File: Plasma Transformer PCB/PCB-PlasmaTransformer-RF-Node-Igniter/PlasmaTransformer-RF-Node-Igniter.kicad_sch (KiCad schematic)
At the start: 66 parts, among them J1 Barrel_Jack_MountingPin, J11 Screw_Terminal_01x01, J12 Screw_Terminal_01x01, J2 Conn_01x02_Pin, J3 Conn_Coaxial, J4 Conn_02x04_Odd_Even, J5 Conn_Coaxial, J8 AudioJack3, M1 Fan, Q1 Q_NMOS_Depletion_GDS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

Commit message: adding PDF schematic
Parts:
- D5, D6, D7, D8: value D_Schottky -> D; symbol Device:D_Schottky -> Device:D; MPN ADS12B3-ASARH -> VS-E7FX0112-M3/I; Manufacturer Luminus Devices -> Vishay
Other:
- note added: "Recommended Resonant Cap: 20cm Globe: 3x 24pF 564RC0GAJ602EJ240J 13cm Globe: 5x 12pF CGP1C120KNSDAAWL25"
- note removed: "Recommended Resonant Cap: 20cm Globe: 2x 24pF 564RC0GAJ602EJ240J 13cm Globe: 5x 12pF CGP1C120KNSDAAWL25"
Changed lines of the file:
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@@
 		)
 	)
-	(text "Recommended Resonant Cap:\n20cm Globe: 2x 24pF 564RC0GAJ602EJ240J\n13cm Globe: 5x 12pF CGP1C120KNSDAAWL25"
+	(text "Recommended Resonant Cap:\n20cm Globe: 3x 24pF 564RC0GAJ602EJ240J\n13cm Globe: 5x 12pF CGP1C120KNSDAAWL25"
 		(exclude_from_sim no)
 		(at 225.806 95.25 0)
@@
 	)
 	(symbol
-		(lib_id "Device:D_Schottky")
+		(lib_id "Device:D")
 		(at 238.76 52.07 0)
 		(unit 1)
@@
 			)
 		)
-		(property "Value" "D_Schottky"
+		(property "Value" "D"
 			(at 238.4425 48.26 0)
 			(effects
@@
 			)
 		)
-		(property "Description" "Schottky diode"
+		(property "Description" "Diode"
+			(at 238.76 52.07 0)
+			(effects
+				(font
+					(size 1.27 1.27)
+				)
+				(hide yes)
+			)
+		)
+		(property "MPN" "VS-E7FX0112-M3/I"
+			(at 239.522 54.61 0)
+			(effects
+				(font
+					(size 1.27 1.27)
+				)
+			)
+		)
+		(property "Manufacturer" "Vishay"
 			(at 238.76 52.07 0)
 			(effects
@@
 			)
 		)
-		(property "MPN" "ADS12B3-ASARH"
+		(property "Sim.Device" "D"
 			(at 238.76 52.07 0)
 			(effects
@@
 			)
 		)
-		(property "Manufacturer" "Luminus Devices"
+		(property "Sim.Pins" "1=K 2=A"
 			(at 238.76 52.07 0)
 			(effects
@@
 	)
 	(symbol
-		(lib_id "Device:D_Schottky")
+		(lib_id "Device:D")
 		(at 238.76 48.26 180)
 		(unit 1)
@@
 			)
 		)
-		(property "Value" "D_Schottky"
+		(property "Value" "D"
 			(at 239.0775 52.07 0)
 			(effects
@@
 			)
 		)
-		(property "Description" "Schottky diode"
+		(property "Description" "Diode"
 			(at 238.76 48.26 0)
 			(effects
@@
 			)
 		)
-		(property "MPN" "ADS12B3-ASARH"
+		(property "MPN" "VS-E7FX0112-M3/I"
 			(at 238.76 48.26 0)
 			(effects
@@
 			)
 		)
-		(property "Manufacturer" "Luminus Devices"
+		(property "Manufacturer" "Vishay"
+			(at 238.76 48.26 0)
+			(effects
+				(font
+					(size 1.27 1.27)
+				)
+				(hide yes)
+			)
+		)
+		(property "Sim.Device" "D"
+			(at 238.76 48.26 0)
+			(effects
+				(font
+					(size 1.27 1.27)
+				)
+				(hide yes)
+			)
+		)
+		(property "Sim.Pins" "1=K 2=A"
 			(at 238.76 48.26 0)
 			(effects
@@
 	)
 	(symbol
-		(lib_id "Device:D_Schottky")
+		(lib_id "Device:D")
 		(at 238.76 44.45 180)
 		(unit 1)
@@
 			)
 		)
-		(property "Value" "D_Schottky"
+		(property "Value" "D"
 			(at 239.0775 48.26 0)
 			(effects
@@
 			)
 		)
-		(property "Description" "Schottky diode"
+		(property "Description" "Diode"
+			(at 238.76 44.45 0)
+			(effects
+				(font
+					(size 1.27 1.27)
+				)
+				(hide yes)
+			)
+		)
+		(property "MPN" "VS-E7FX0112-M3/I"
+			(at 238.76 44.45 0)
+			(effects
+				(font
+					(size 1.27 1.27)
+				)
+				(hide yes)
+			)
+		)
+		(property "Manufacturer" "Vishay"
 			(at 238.76 44.45 0)
 			(effects
@@
 			)
 		)
-		(property "MPN" "ADS12B3-ASARH"
+		(property "Sim.Device" "D"
 			(at 238.76 44.45 0)
 			(effects
@@
 			)
 		)
-		(property "Manufacturer" "Luminus Devices"
+		(property "Sim.Pins" "1=K 2=A"
 			(at 238.76 44.45 0)
 			(effects
@@
 	)
 	(symbol
-		(lib_id "Device:D_Schottky")
+		(lib_id "Device:D")
 		(at 238.76 40.64 0)
 		(unit 1)
@@
 			)
 		)
-		(property "Value" "D_Schottky"
+		(property "Value" "D"
 			(at 238.4425 36.83 0)
 			(effects
@@
 			)
 		)
-		(property "Description" "Schottky diode"
+		(property "Description" "Diode"
 			(at 238.76 40.64 0)
 			(effects
@@
 			)
 		)
-		(property "MPN" "ADS12B3-ASARH"
+		(property "MPN" "VS-E7FX0112-M3/I"
+			(at 238.76 40.64 0)
+			(effects
+				(font
+					(size 1.27 1.27)
+				)
+				(hide yes)
+			)
+		)
+		(property "Manufacturer" "Vishay"
 			(at 238.76 40.64 0)
 			(effects
@@
 			)
 		)
-		(property "Manufacturer" "Luminus Devices"
+		(property "Sim.Device" "D"
+			(at 238.76 40.64 0)
+			(effects
+				(font
+					(size 1.27 1.27)
+				)
+				(hide yes)
+			)
+		)
+		(property "Sim.Pins" "1=K 2=A"
 			(at 238.76 40.64 0)
 			(effects

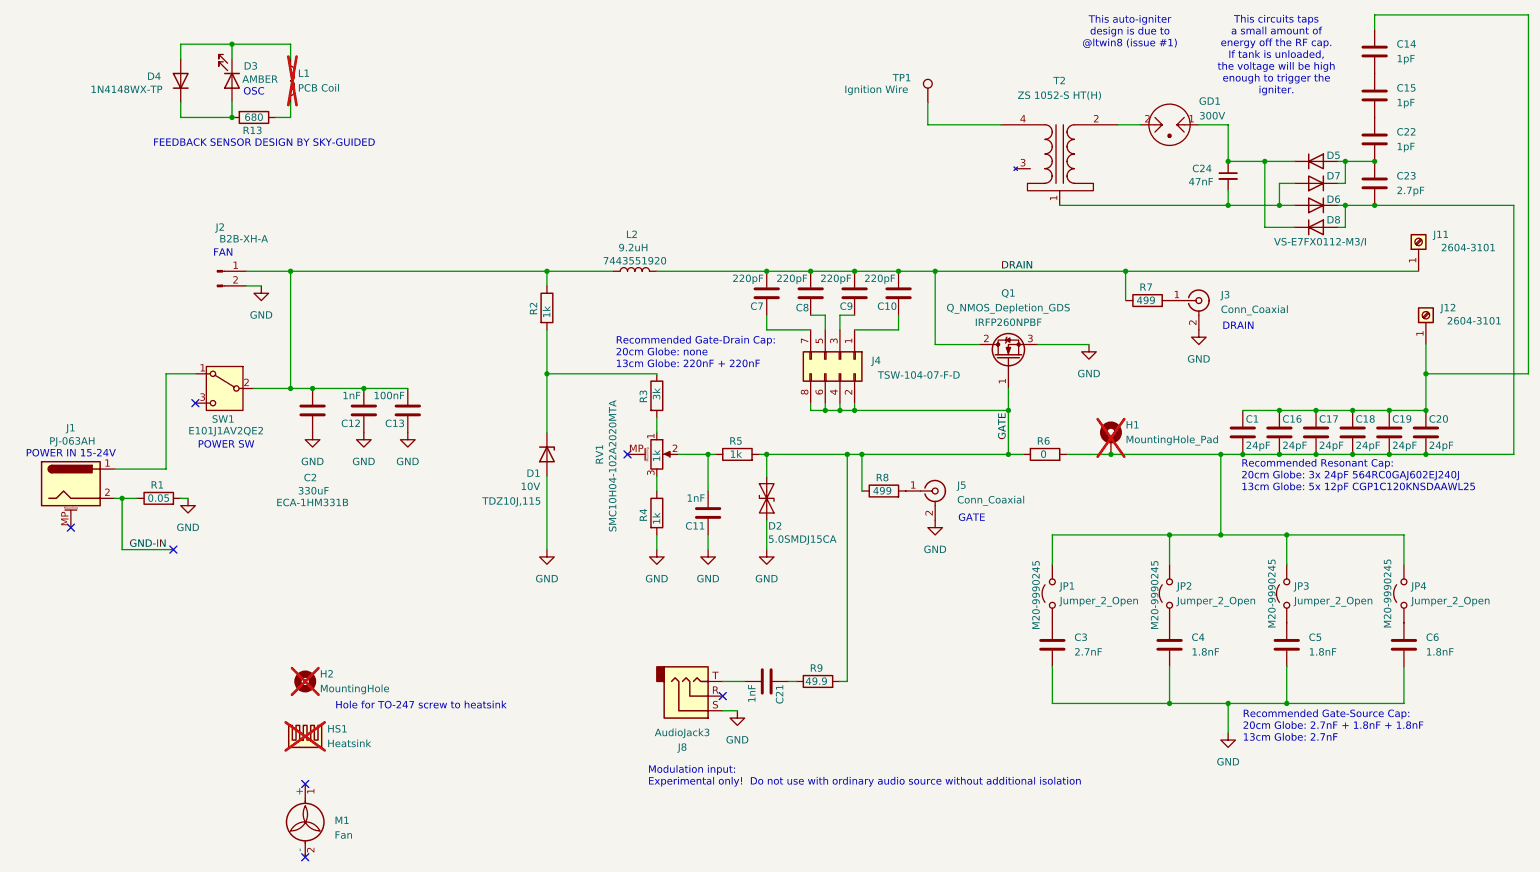
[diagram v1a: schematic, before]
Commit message: layout updates for Rev 3B > Rev 4: gate selector caps, SMD footprint for trigger coil, silkscreen updates
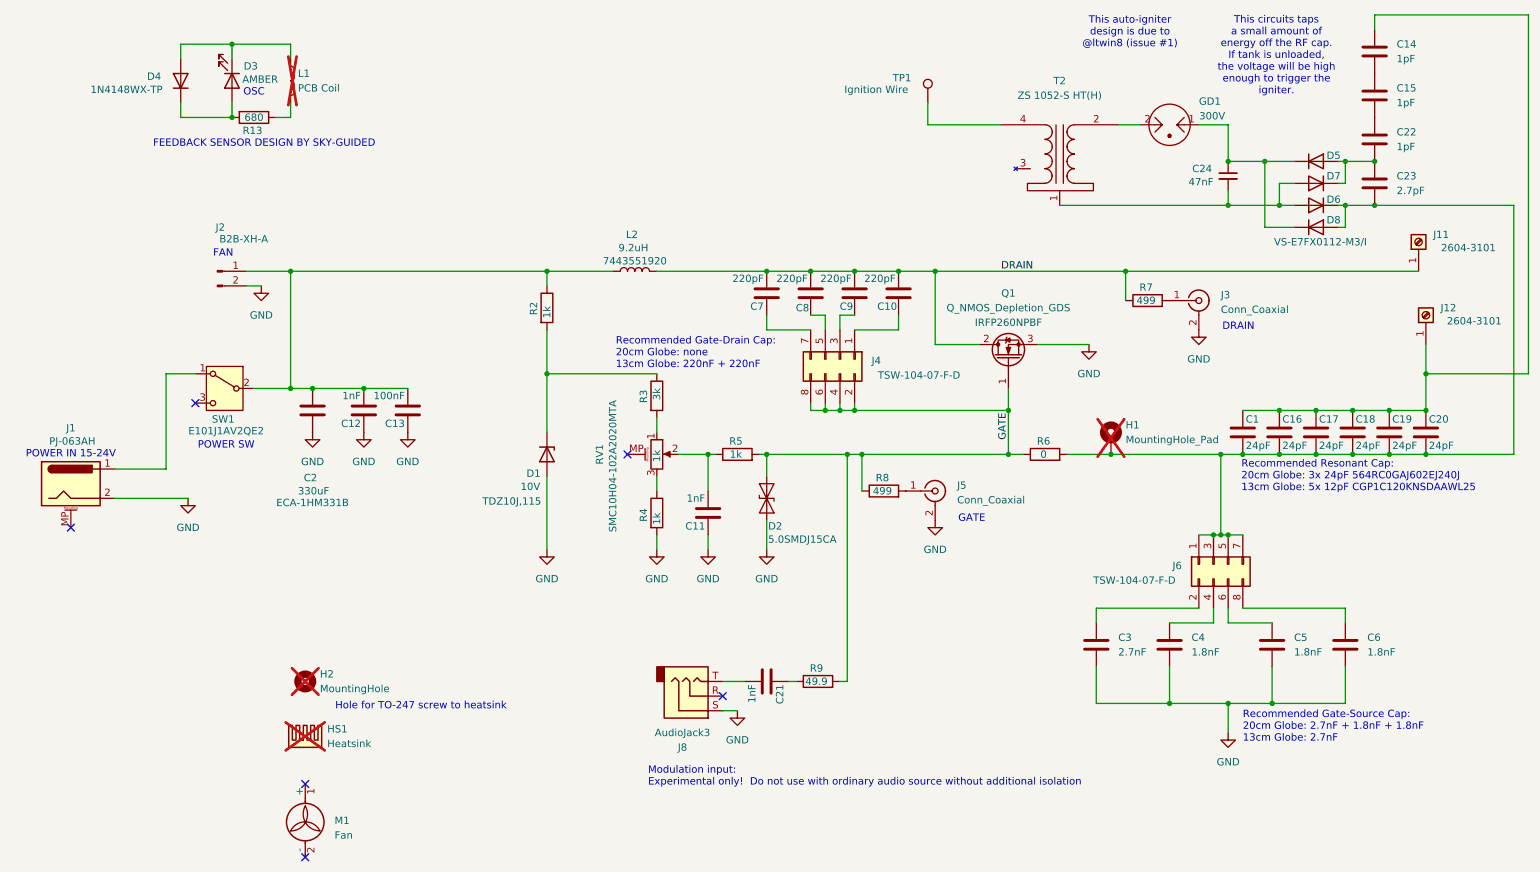
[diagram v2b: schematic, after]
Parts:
- removed JP1, JP2, JP3, JP4: Jumper_2_Open, Connector_PinHeader_2.54mm:PinHeader_1x02_P2.54mm_Vertical, symbol Jumper:Jumper_2_Open
- removed R1: 0.05, Resistor_SMD:R_2512_6332Metric, symbol Device:R
- added J6: Conn_02x04_Odd_Even, Connector_PinHeader_2.54mm:PinHeader_2x04_P2.54mm_Vertical, symbol Connector_Generic:Conn_02x04_Odd_Even
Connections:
- net GND-IN is gone; now on net GND: J1.2
- net at C6.1: now also J6.8 (Pin_8)
- net at C1.2, C16.2, C17.2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: now also J6.1 (Pin_1), J6.3 (Pin_3), J6.5 (Pin_5), J6.7 (Pin_7)
- net at C5.1: now also J6.6 (Pin_6)
- net at C4.1: now also J6.4 (Pin_4)
- net at C3.1: now also J6.2 (Pin_2)
- no-connect marks 7 -> 6
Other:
- moved on the sheet: C3, C5, C6

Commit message: 13cm V2 design WIP, updates to Rev 4 PCB
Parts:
- added T1: BO-02, ALibrary:BO-02, symbol ALibrary:BO-02
- added TP2, TP3: Choke, Connector_Wire:SolderWire-1sqmm_1x01_D1.4mm_OD2.7mm, symbol Connector:TestPoint
- D4: now not fitted
- L2: value 9.2uH -> 30uH; footprint Inductor_SMD:L_APV_APH1770 -> ALibrary:B82559B_TDK; MPN 7443551920 -> B82559B0303A016
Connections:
- net DRAIN: now also TP3.1
- net at GD1.2, T2.2 (AA): now also T1.1 (Primary)
- net at C12.2, C13.2, C2.1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: now also TP2.1
- net at C24.2, D6.2 (A), D7.2 (A)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: now also T1.2 (AB)
- net at T2.4 (SB), TP1.1: now also T1.3 (Secondary)
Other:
- note added: "Alternate either SMD or Air Core choke"
- note added: "Alternate trigger: BO-02"
